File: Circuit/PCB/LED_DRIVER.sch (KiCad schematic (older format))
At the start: 5 parts, among them U8 CL6807

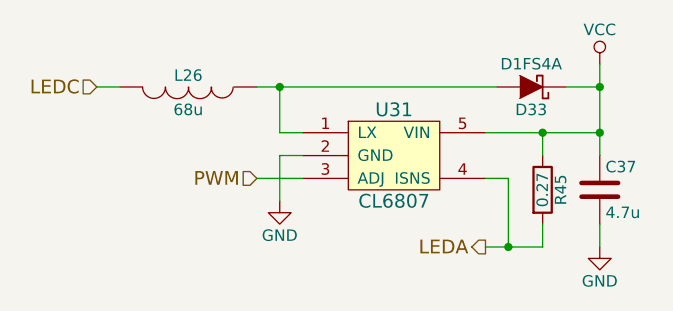
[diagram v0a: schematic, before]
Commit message: CvPcb settled
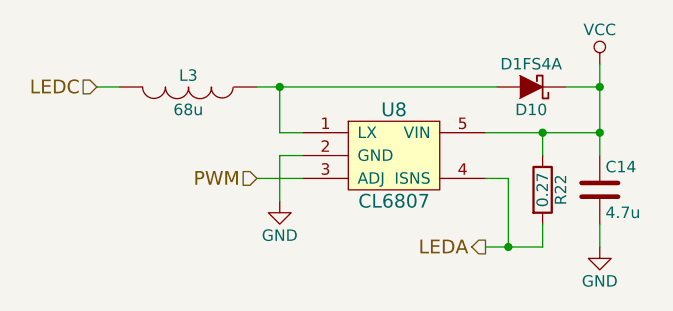
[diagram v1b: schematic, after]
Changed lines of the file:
@@
 $Descr A4 11693 8268
 encoding utf-8
-Sheet 15 26
+Sheet 3 26
 Title ""
 Date ""
@@
 AR Path="/55ECF96D/55EC5EE0" Ref="#PWR0102"  Part="1"
 AR Path="/55ECF972/55EC5EE0" Ref="#PWR0105"  Part="1"
-F 0 "#PWR0105" H 2650 2300 50  0001 C CNN
+F 0 "#PWR036" H 2650 2300 50  0001 C CNN
 F 1 "GND" H 2650 2400 50  0000 C CNN
 F 2 "" H 2650 2550 60  0000 C CNN
@@
 AR Path="/55ECF96D/55EC5EF4" Ref="#PWR0103"  Part="1"
 AR Path="/55ECF972/55EC5EF4" Ref="#PWR0106"  Part="1"
-F 0 "#PWR0106" H 4050 1800 50  0001 C CNN
+F 0 "#PWR037" H 4050 1800 50  0001 C CNN
 F 1 "VCC" H 4050 2100 50  0000 C CNN
 F 2 "" H 4050 1950 60  0000 C CNN
@@
 AR Path="/55ECF96D/55EC6028" Ref="U30"  Part="1"
 AR Path="/55ECF972/55EC6028" Ref="U31"  Part="1"
-F 0 "U31" H 3150 2550 60  0000 C CNN
+F 0 "U8" H 3150 2550 60  0000 C CNN
 F 1 "CL6807" H 3150 2150 60  0000 C CNN
 F 2 "Housings_SOT-89:SOT89-5_Housing_Handsoldering" H 3100 2300 60  0001 C CNN
@@
 AR Path="/55ECF96D/55EC62FB" Ref="L25"  Part="1"
 AR Path="/55ECF972/55EC62FB" Ref="L26"  Part="1"
-F 0 "L26" V 2200 2050 50  0000 C CNN
+F 0 "L3" V 2200 2050 50  0000 C CNN
 F 1 "68u" V 2350 2050 50  0000 C CNN
 F 2 "Choke_SMD:Choke_SMD_10.4x10.4_H4.8" H 2250 2050 60  0001 C CNN
@@
 AR Path="/55ECF96D/55EC639A" Ref="C36"  Part="1"
 AR Path="/55ECF972/55EC639A" Ref="C37"  Part="1"
-F 0 "C37" H 4075 2600 50  0000 L CNN
+F 0 "C14" H 4075 2600 50  0000 L CNN
 F 1 "4.7u" H 4075 2400 50  0000 L CNN
 F 2 "Capacitors_SMD:C_0805_HandSoldering" H 4088 2350 30  0001 C CNN
@@
 AR Path="/55ECF96D/55EC6949" Ref="#PWR0104"  Part="1"
 AR Path="/55ECF972/55EC6949" Ref="#PWR0107"  Part="1"
-F 0 "#PWR0107" H 4050 2500 50  0001 C CNN
+F 0 "#PWR038" H 4050 2500 50  0001 C CNN
 F 1 "GND" H 4050 2600 50  0000 C CNN
 F 2 "" H 4050 2750 60  0000 C CNN
@@
 AR Path="/55ECF96D/55EC6B8C" Ref="R44"  Part="1"
 AR Path="/55ECF972/55EC6B8C" Ref="R45"  Part="1"
-F 0 "R45" V 3880 2500 50  0000 C CNN
+F 0 "R22" V 3880 2500 50  0000 C CNN
 F 1 "0.27" V 3800 2500 50  0000 C CNN
 F 2 "Resistors_SMD:R_1206_HandSoldering" V 3730 2500 30  0001 C CNN
@@
 AR Path="/55ECF96D/55EC6E68" Ref="D32"  Part="1"
 AR Path="/55ECF972/55EC6E68" Ref="D33"  Part="1"
-F 0 "D33" H 3750 2150 50  0000 C CNN
+F 0 "D10" H 3750 2150 50  0000 C CNN
 F 1 "D1FS4A" H 3750 1950 50  0000 C CNN
 F 2 "Diodes_SMD:SMB_Handsoldering" H 3750 2050 60  0001 C CNN

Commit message: update pcb
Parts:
- C14: footprint Capacitors_SMD:C_0805_HandSoldering -> Capacitors_SMD:C_0805
- D10: footprint Diodes_SMD:SMB_Handsoldering -> Diodes_SMD:SMB_Standard
- R22: footprint Resistors_SMD:R_1206_HandSoldering -> Resistors_SMD:R_1206
- U8: footprint Housings_SOT-89:SOT89-5_Housing_Handsoldering -> Housings_SOT-89:SOT89-5_Housing
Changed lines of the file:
@@
 AR Path="/55ECF96D/55EC5EE0" Ref="#PWR0102"  Part="1"
 AR Path="/55ECF972/55EC5EE0" Ref="#PWR0105"  Part="1"
-F 0 "#PWR036" H 2650 2300 50  0001 C CNN
+F 0 "#PWR087" H 2650 2300 50  0001 C CNN
 F 1 "GND" H 2650 2400 50  0000 C CNN
 F 2 "" H 2650 2550 60  0000 C CNN
@@
 AR Path="/55ECF96D/55EC5EF4" Ref="#PWR0103"  Part="1"
 AR Path="/55ECF972/55EC5EF4" Ref="#PWR0106"  Part="1"
-F 0 "#PWR037" H 4050 1800 50  0001 C CNN
+F 0 "#PWR088" H 4050 1800 50  0001 C CNN
 F 1 "VCC" H 4050 2100 50  0000 C CNN
 F 2 "" H 4050 1950 60  0000 C CNN
@@
 AR Path="/55ECF96D/55EC6028" Ref="U30"  Part="1"
 AR Path="/55ECF972/55EC6028" Ref="U31"  Part="1"
-F 0 "U8" H 3150 2550 60  0000 C CNN
+F 0 "U25" H 3150 2550 60  0000 C CNN
 F 1 "CL6807" H 3150 2150 60  0000 C CNN
-F 2 "Housings_SOT-89:SOT89-5_Housing_Handsoldering" H 3100 2300 60  0001 C CNN
+F 2 "Housings_SOT-89:SOT89-5_Housing" H 3100 2300 60  0001 C CNN
 F 3 "" H 3100 2300 60  0000 C CNN
 	1    3150 2350
@@
 AR Path="/55ECF96D/55EC62FB" Ref="L25"  Part="1"
 AR Path="/55ECF972/55EC62FB" Ref="L26"  Part="1"
-F 0 "L3" V 2200 2050 50  0000 C CNN
+F 0 "L20" V 2200 2050 50  0000 C CNN
 F 1 "68u" V 2350 2050 50  0000 C CNN
 F 2 "Choke_SMD:Choke_SMD_10.4x10.4_H4.8" H 2250 2050 60  0001 C CNN
@@
 AR Path="/55ECF96D/55EC639A" Ref="C36"  Part="1"
 AR Path="/55ECF972/55EC639A" Ref="C37"  Part="1"
-F 0 "C14" H 4075 2600 50  0000 L CNN
+F 0 "C31" H 4075 2600 50  0000 L CNN
 F 1 "4.7u" H 4075 2400 50  0000 L CNN
-F 2 "Capacitors_SMD:C_0805_HandSoldering" H 4088 2350 30  0001 C CNN
+F 2 "Capacitors_SMD:C_0805" H 4088 2350 30  0001 C CNN
 F 3 "" H 4050 2500 60  0000 C CNN
 	1    4050 2500
@@
 AR Path="/55ECF96D/55EC6949" Ref="#PWR0104"  Part="1"
 AR Path="/55ECF972/55EC6949" Ref="#PWR0107"  Part="1"
-F 0 "#PWR038" H 4050 2500 50  0001 C CNN
+F 0 "#PWR089" H 4050 2500 50  0001 C CNN
 F 1 "GND" H 4050 2600 50  0000 C CNN
 F 2 "" H 4050 2750 60  0000 C CNN
@@
 AR Path="/55ECF96D/55EC6B8C" Ref="R44"  Part="1"
 AR Path="/55ECF972/55EC6B8C" Ref="R45"  Part="1"
-F 0 "R22" V 3880 2500 50  0000 C CNN
+F 0 "R39" V 3880 2500 50  0000 C CNN
 F 1 "0.27" V 3800 2500 50  0000 C CNN
-F 2 "Resistors_SMD:R_1206_HandSoldering" V 3730 2500 30  0001 C CNN
+F 2 "Resistors_SMD:R_1206" V 3730 2500 30  0001 C CNN
 F 3 "" H 3800 2500 30  0000 C CNN
 	1    3800 2500
@@
 AR Path="/55ECF96D/55EC6E68" Ref="D32"  Part="1"
 AR Path="/55ECF972/55EC6E68" Ref="D33"  Part="1"
-F 0 "D10" H 3750 2150 50  0000 C CNN
+F 0 "D27" H 3750 2150 50  0000 C CNN
 F 1 "D1FS4A" H 3750 1950 50  0000 C CNN
-F 2 "Diodes_SMD:SMB_Handsoldering" H 3750 2050 60  0001 C CNN
+F 2 "Diodes_SMD:SMB_Standard" H 3750 2050 60  0001 C CNN
 F 3 "" H 3750 2050 60  0000 C CNN
 	1    3750 2050
